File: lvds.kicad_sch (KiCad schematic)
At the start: 33 parts, among them J9 Conn_01x34_Female, U10 TPS61176RTER, U11 TCA9802, U12 NTB0102, U13 MIC5504-1.8YM5, U5 SN65DSI83TPAPRQ1

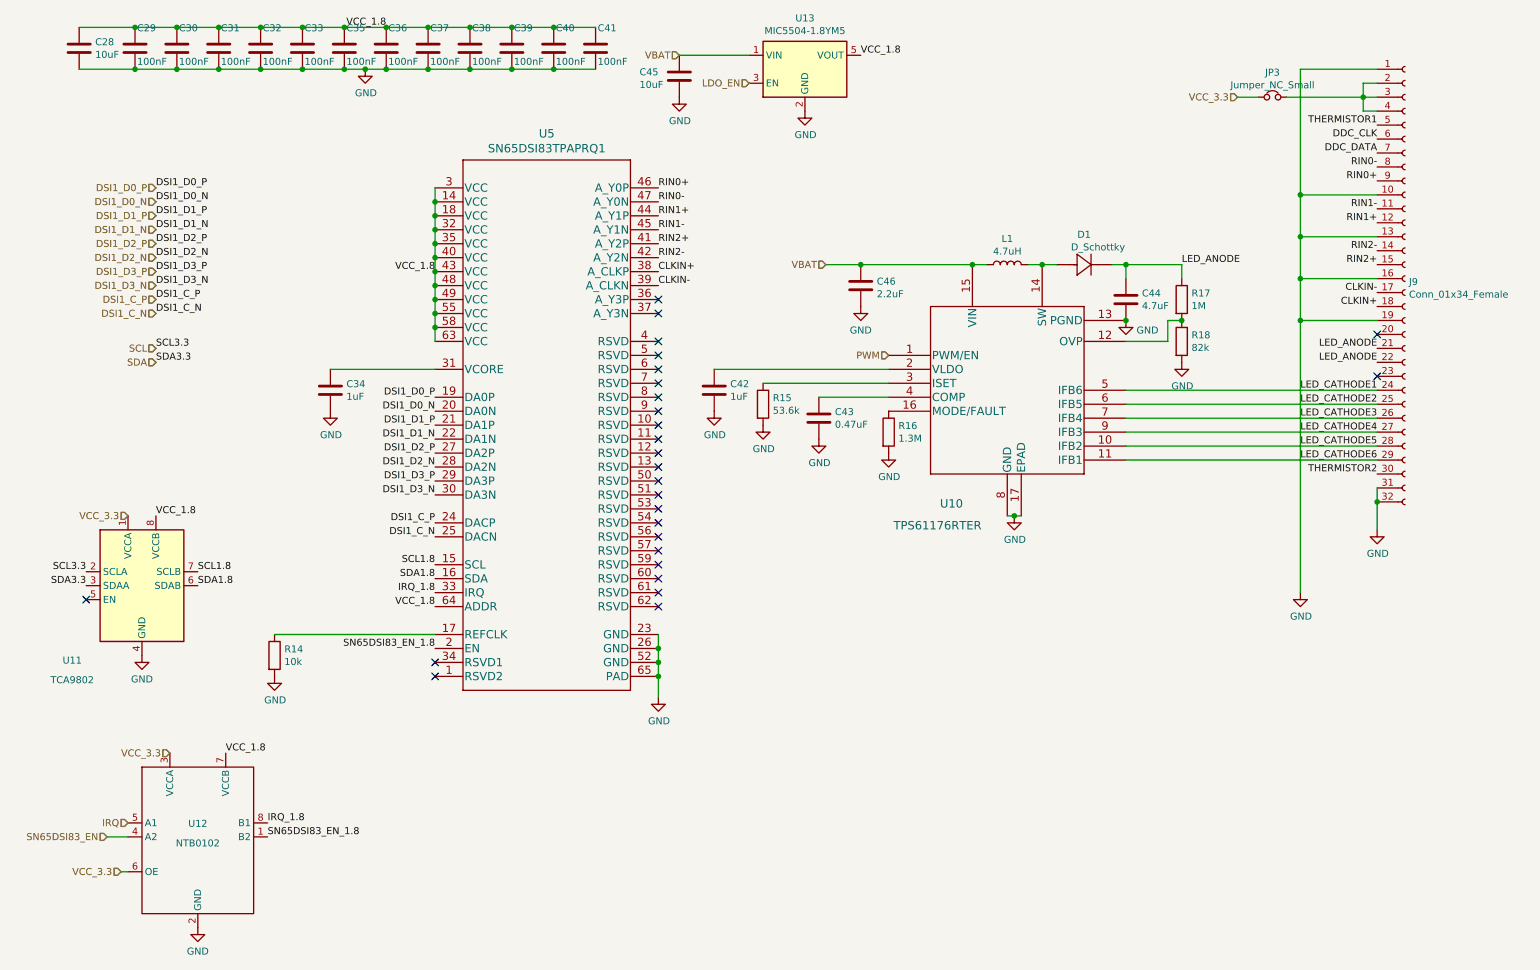
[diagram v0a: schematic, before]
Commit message: Route CM4 board with differential connector on the right.
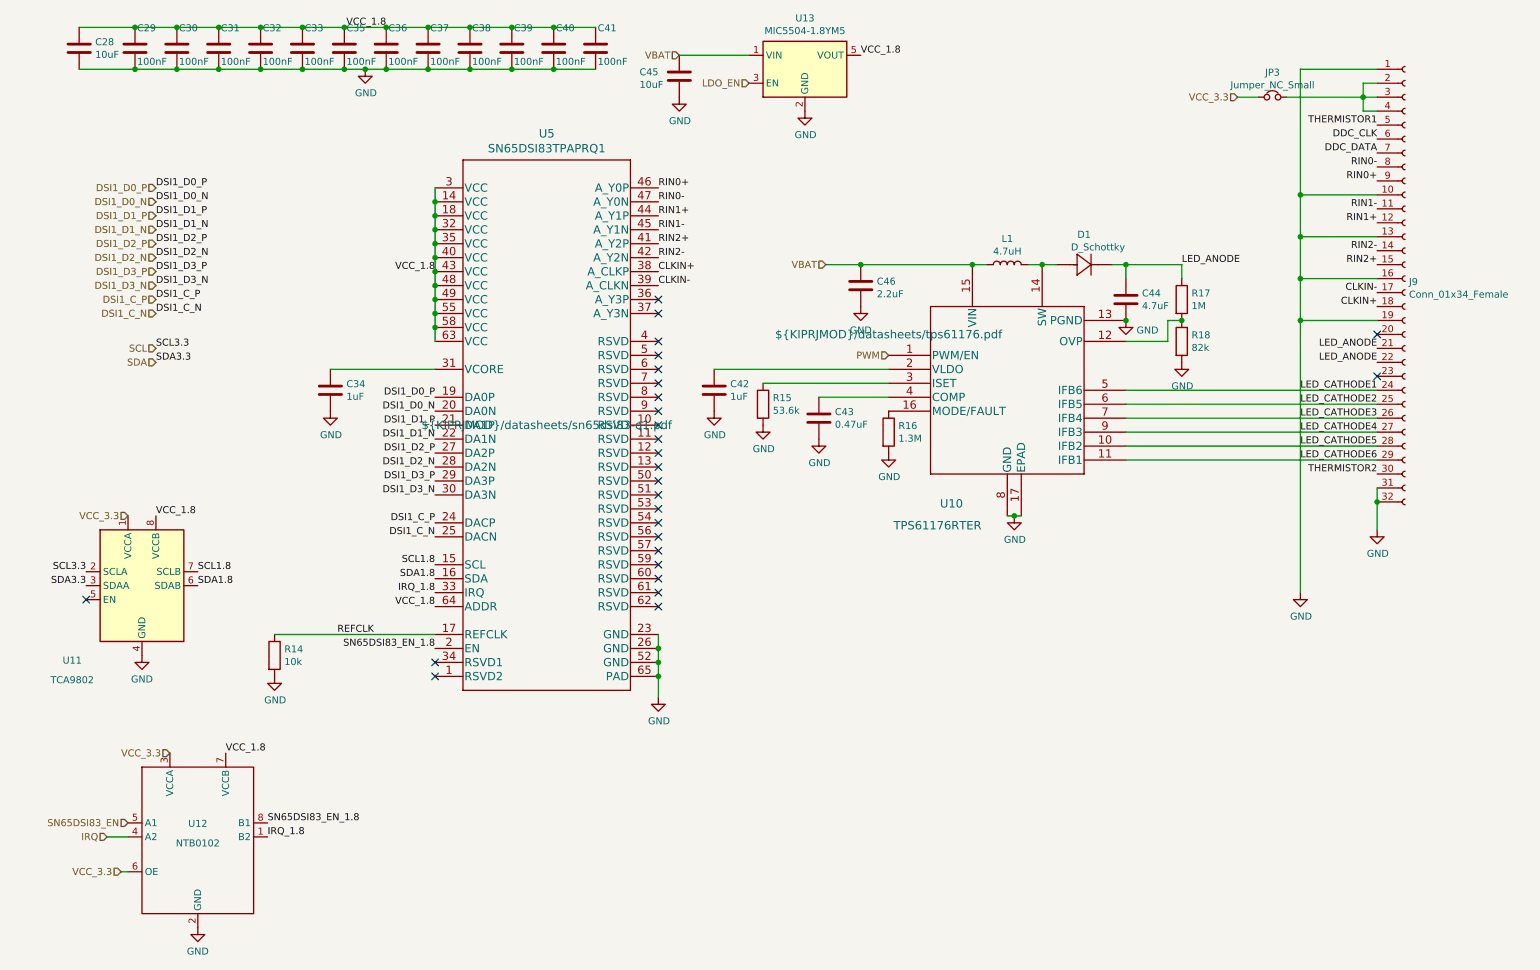
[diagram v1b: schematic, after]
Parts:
- C44: footprint Capacitor_SMD:C_0603_1608Metric -> Capacitor_SMD:C_0402_1005Metric
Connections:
- net IRQ: now also U12.4 (A2); no longer U12.5 (A1)
- net IRQ_1.8: now also U12.1 (B2); no longer U12.8 (B1)
- net SN65DSI83_EN: now also U12.5 (A1); no longer U12.4 (A2)
- net SN65DSI83_EN_1.8: now also U12.8 (B1); no longer U12.1 (B2)
- net REFCLK: now reaches R14.1, U5.17 (REFCLK)

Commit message: Switch tps61176 for tps61177, since 61176 is out of stock. Also finish fixing hole clearance violations.
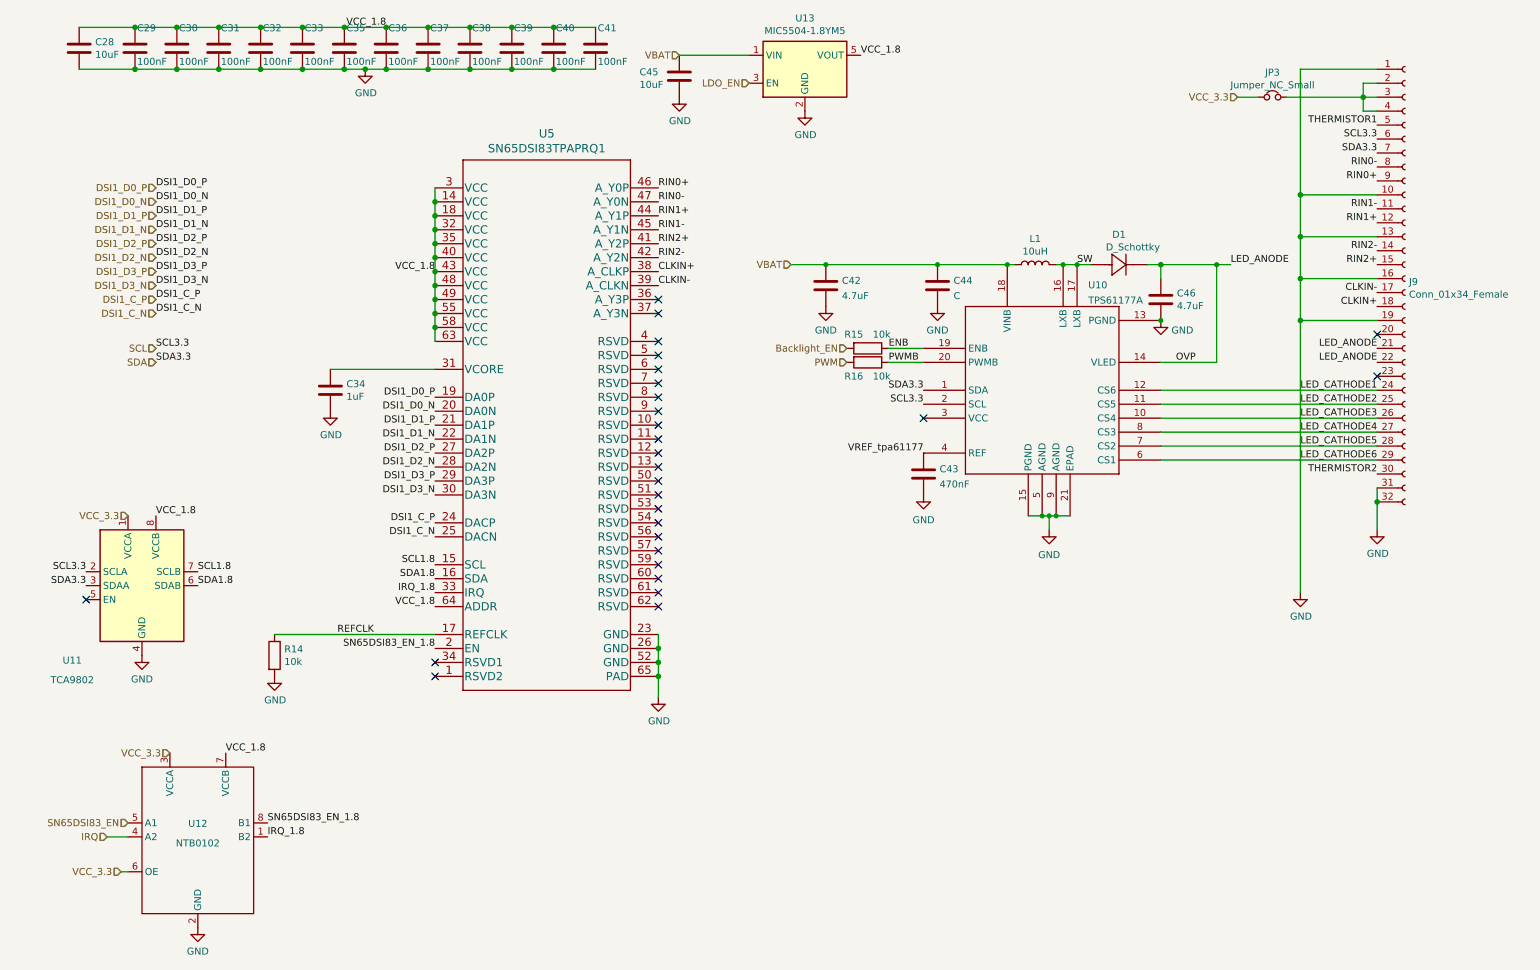
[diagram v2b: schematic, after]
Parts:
- removed R17: 1M, Resistor_SMD:R_0402_1005Metric, symbol Device:R
- removed R18: 82k, Resistor_SMD:R_0402_1005Metric, symbol Device:R
- removed U10: TPS61176RTER, footprints:TPS61176RTER, symbol TPS61176RTER:TPS61176RTER
- added U10: TPS61177A, footprints:tps61177a, symbol tps61177:TPS61177A
- C42: value 1uF -> 4.7uF; footprint Capacitor_SMD:C_0402_1005Metric -> Capacitor_SMD:C_0805_2012Metric
- C43: value 0.47uF -> 470nF
- C44: value 4.7uF -> C
- C46: value 2.2uF -> 4.7uF; footprint Capacitor_SMD:C_0402_1005Metric -> Capacitor_SMD:C_0805_2012Metric
- D1: footprint footprints:PMEG4010EPK_315 -> footprints:sba0450q
- L1: value 4.7uH -> 10uH; footprint Inductor_SMD:L_0805_2012Metric -> footprints:LQH3NPZ100MGRL; Digi-Key PN MLZ2012N4R7LT000 -> 490-15956-1-ND
- R15: value 53.6k -> 10k
- R16: value 1.3M -> 10k
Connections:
- net DDC_CLK is gone; now on net SCL: J9.6 (Pin_6)
- net DDC_DATA is gone; now on net SDA: J9.7 (Pin_7)
- net GND: now also U10.13 (PGND), U10.15 (PGND), U10.21 (EPAD), U10.5 (AGND), U10.9 (AGND); no longer R15.2, R16.2
- net LED_ANODE: now also C46.1, U10.14 (VLED); no longer C44.1
- net LED_CATHODE1: now also U10.12 (CS6)
- net LED_CATHODE2: now also U10.11 (CS5)
- net LED_CATHODE3: now also U10.10 (CS4)
- net LED_CATHODE4: now also U10.8 (CS3)
- net LED_CATHODE5: now also U10.7 (CS2)
- net LED_CATHODE6: now also U10.6 (CS1)
- net PWM: now also R16.2
- net SCL: now also U10.2 (SCL)
- net SDA: now also U10.1 (SDA)
- net VBAT: now also C42.1, C44.1, U10.18 (VINB); no longer C46.1
- net SW: now reaches D1.2, L1.2
- net SW: now also U10.16 (LXB), U10.17 (LXB)
- net PWMB: now reaches R16.1
- net PWMB: now also U10.20 (PWMB)
- net ENB: now reaches R15.1
- net ENB: now also U10.19 (ENB)
- net VREF_tpa61177: now reaches C43.1
- net VREF_tpa61177: now also U10.4 (REF)
- new net Backlight_EN: R15.2
- no-connect marks 27 -> 28

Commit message: Start re-routing CM4 board with most parts on the back layer, and CM4 itself turned around so that the BCM2711 is in a deeper part of the iPad case.
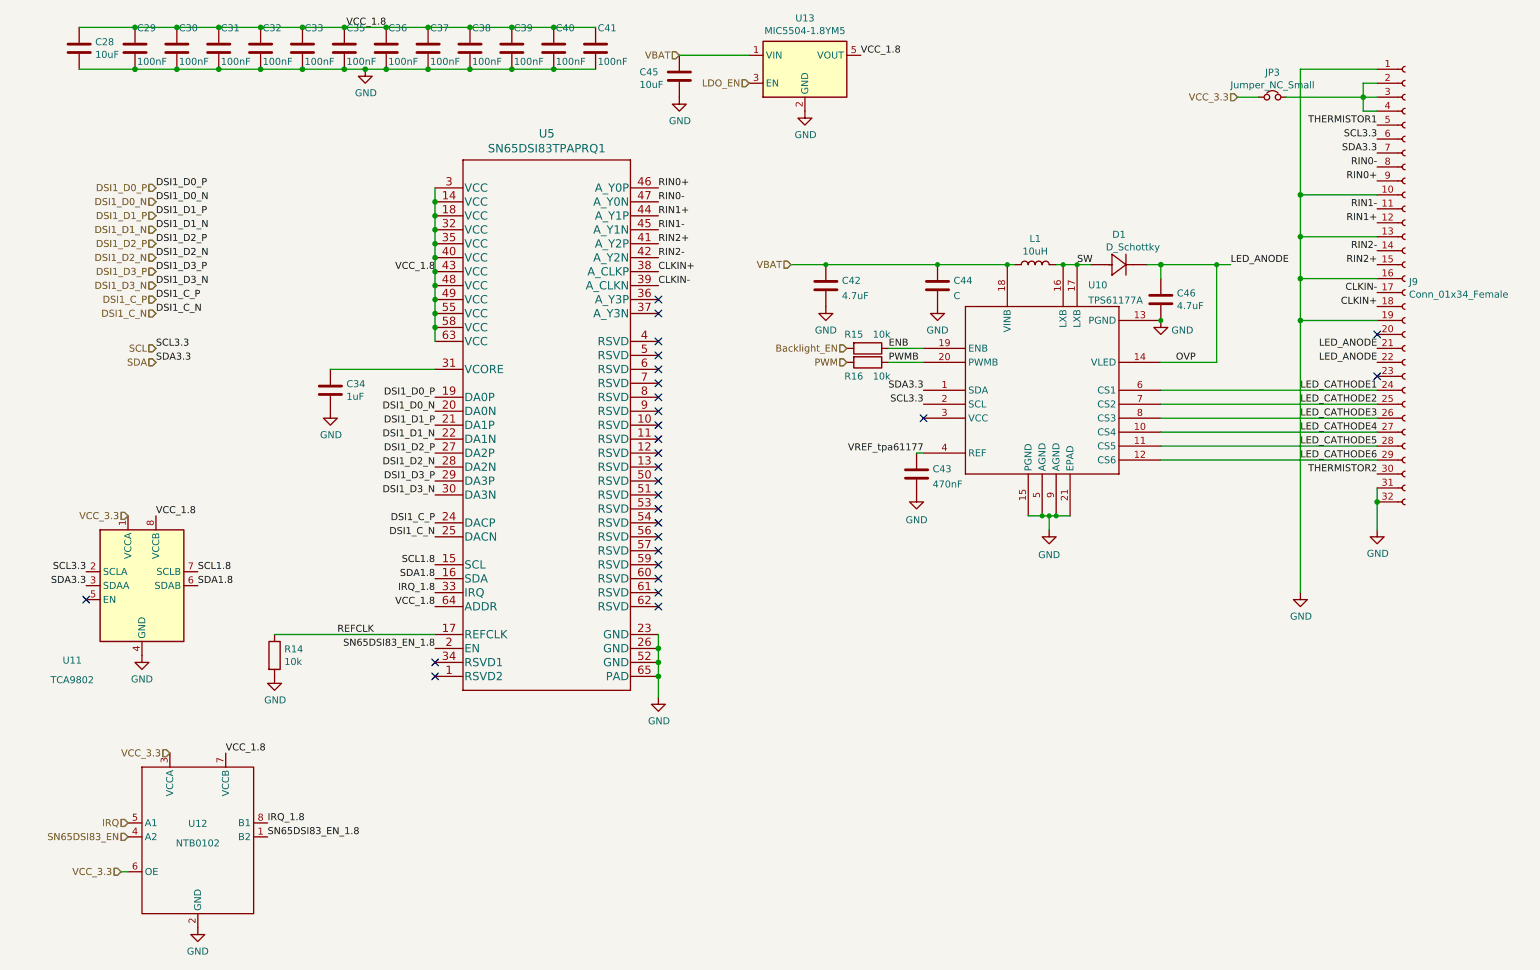
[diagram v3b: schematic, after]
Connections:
- net IRQ: now also U12.5 (A1); no longer U12.4 (A2)
- net IRQ_1.8: now also U12.8 (B1); no longer U12.1 (B2)
- net LED_CATHODE1: now also U10.6 (CS1); no longer U10.12 (CS6)
- net LED_CATHODE2: now also U10.7 (CS2); no longer U10.11 (CS5)
- net LED_CATHODE3: now also U10.8 (CS3); no longer U10.10 (CS4)
- net LED_CATHODE4: now also U10.10 (CS4); no longer U10.8 (CS3)
- net LED_CATHODE5: now also U10.11 (CS5); no longer U10.7 (CS2)
- net LED_CATHODE6: now also U10.12 (CS6); no longer U10.6 (CS1)
- net SN65DSI83_EN: now also U12.4 (A2); no longer U12.5 (A1)
- net SN65DSI83_EN_1.8: now also U12.1 (B2); no longer U12.8 (B1)
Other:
- moved on the sheet: C43
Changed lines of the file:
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@@
     (stroke (width 0) (type solid) (color 0 0 0 0))
   )
-  (wire (pts (xy 30.48 168.91) (xy 34.29 168.91))
-    (stroke (width 0) (type solid) (color 0 0 0 0))
+  (wire (pts (xy 177.8 99.06) (xy 179.07 99.06))
+    (stroke (width 0) (type default) (color 0 0 0 0))
   )
   (wire (pts (xy 161.29 64.77) (xy 181.61 64.77))
@@
     (effects (font (size 1.27 1.27)) (justify right bottom))
   )
-  (label "SN65DSI83_EN_1.8" (at 59.69 166.37 0)
+  (label "SN65DSI83_EN_1.8" (at 59.69 168.91 0)
     (effects (font (size 1.27 1.27)) (justify left bottom))
   )
@@
     (effects (font (size 1.27 1.27)) (justify left bottom))
   )
-  (label "IRQ_1.8" (at 59.69 168.91 0)
+  (label "IRQ_1.8" (at 59.69 166.37 0)
     (effects (font (size 1.27 1.27)) (justify left bottom))
   )
@@
     (effects (font (size 1.27 1.27)) (justify right))
   )
-  (hierarchical_label "IRQ" (shape input) (at 30.48 168.91 180)
+  (hierarchical_label "IRQ" (shape input) (at 34.29 166.37 180)
     (effects (font (size 1.27 1.27)) (justify right))
   )
@@
     (effects (font (size 1.27 1.27)) (justify right))
   )
-  (hierarchical_label "SN65DSI83_EN" (shape input) (at 34.29 166.37 180)
+  (hierarchical_label "SN65DSI83_EN" (shape input) (at 34.29 168.91 180)
     (effects (font (size 1.27 1.27)) (justify right))
   )
@@
     (pin "8")
   )
-  (symbol (lib_id "Device:C") (at 179.07 102.87 0) (unit 1)
+  (symbol (lib_id "Device:C") (at 177.8 102.87 0) (unit 1)
     (in_bom yes) (on_board yes) (fields_autoplaced)
-    (property "Reference" "C43" (id 0) (at 181.991 101.9615 0)
-      (effects (font (size 1.27 1.27)) (justify left))
-    )
-    (property "Value" "470nF" (id 1) (at 181.991 104.7366 0)
-      (effects (font (size 1.27 1.27)) (justify left))
-    )
-    (property "Footprint" "Capacitor_SMD:C_0402_1005Metric" (id 2) (at 180.0352 106.68 0)
-      (effects (font (size 1.27 1.27)) hide)
-    )
-    (property "Datasheet" "~" (id 3) (at 179.07 102.87 0)
+    (property "Reference" "C43" (id 0) (at 180.721 101.9615 0)
+      (effects (font (size 1.27 1.27)) (justify left))
+    )
+    (property "Value" "470nF" (id 1) (at 180.721 104.7366 0)
+      (effects (font (size 1.27 1.27)) (justify left))
+    )
+    (property "Footprint" "Capacitor_SMD:C_0402_1005Metric" (id 2) (at 178.7652 106.68 0)
+      (effects (font (size 1.27 1.27)) hide)
+    )
+    (property "Datasheet" "~" (id 3) (at 177.8 102.87 0)
       (effects (font (size 1.27 1.27)) hide)
     )
@@
     (pin "2")
   )
-  (symbol (lib_id "power:GND") (at 179.07 106.68 0) (unit 1)
+  (symbol (lib_id "power:GND") (at 177.8 106.68 0) (unit 1)
     (in_bom yes) (on_board yes) (fields_autoplaced)
-    (property "Reference" "#PWR0148" (id 0) (at 179.07 113.03 0)
-      (effects (font (size 1.27 1.27)) hide)
-    )
-    (property "Value" "GND" (id 1) (at 179.07 111.2425 0))
-    (property "Footprint" "" (id 2) (at 179.07 106.68 0)
-      (effects (font (size 1.27 1.27)) hide)
-    )
-    (property "Datasheet" "" (id 3) (at 179.07 106.68 0)
-      (effects (font (size 1.27 1.27)) hide)
-    )
+    (property "Reference" "#PWR0148" (id 0) (at 177.8 113.03 0)
+      (effects (font (size 1.27 1.27)) hide)
+    )
+    (property "Value" "GND" (id 1) (at 177.8 111.2425 0))
+    (property "Footprint" "" (id 2) (at 177.8 106.68 0)
+      (effects (font (size 1.27 1.27)) hide)
+    )
+    (property "Datasheet" "" (id 3) (at 177.8 106.68 0)
+      (effects (font (size 1.27 1.27)) hide)
+    )
